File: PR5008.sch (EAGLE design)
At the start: 48 parts

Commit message: beginnings of changes
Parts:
- removed C17: 470pf, resistor:C-USC0805
- removed JP1: (no value), SparkFun-Connectors:M05LOCK
- added C21: 470pF, resistor:C-USC0603
- added JP2: (no value), SparkFun-Connectors:M03LOCK
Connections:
- net GND: now also C21.1, JP2.2; no longer C17.2, JP1.4
- net N$12: now also JP2.1; no longer JP1.3
- net N$22: no longer JP1.1
- net N$29: no longer JP1.2
- net N$34: now also C21.2; no longer C17.1
- net VCC: now also JP2.3; no longer JP1.5
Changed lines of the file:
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@@
 <part name="C16" library="resistor" deviceset="C-US" device="C0603" value="2.2uF"/>
 <part name="GND16" library="SparkFun-Aesthetics" deviceset="GND" device=""/>
-<part name="C17" library="resistor" deviceset="C-US" device="C0805" value="470pf"/>
 <part name="R13" library="resistor" deviceset="R-US_" device="R0603" value="0Ohm"/>
 <part name="GND17" library="SparkFun-Aesthetics" deviceset="GND" device=""/>
@@
 <part name="U$4" library="PR_Libraries" deviceset="SI4831_FM_IC" device=""/>
 <part name="GND18" library="SparkFun-Aesthetics" deviceset="GND" device=""/>
-<part name="JP1" library="SparkFun-Connectors" deviceset="M05" device="LOCK"/>
 <part name="GND19" library="SparkFun-Aesthetics" deviceset="GND" device=""/>
 <part name="P+7" library="supply1" deviceset="VCC" device=""/>
+<part name="JP2" library="SparkFun-Connectors" deviceset="M03" device="LOCK"/>
+<part name="C21" library="resistor" deviceset="C-US" device="C0603" value="470pF"/>
 </parts>
 <sheets>
@@
 </instance>
 <instance part="GND8" gate="1" x="-5.08" y="33.274"/>
-<instance part="GND9" gate="1" x="10.16" y="53.086"/>
+<instance part="GND9" gate="1" x="12.7" y="50.8"/>
 <instance part="L2" gate="G$1" x="84.582" y="76.2" smashed="yes" rot="R270">
 <attribute name="NAME" x="84.582" y="77.978" size="1.778" layer="95" rot="R180"/>
@@
 <instance part="C16" gate="G$1" x="59.436" y="97.536" rot="R90"/>
 <instance part="GND16" gate="1" x="161.798" y="43.18"/>
-<instance part="C17" gate="G$1" x="72.136" y="27.686" smashed="yes">
-<attribute name="NAME" x="65.024" y="28.067" size="1.778" layer="95"/>
-<attribute name="VALUE" x="64.516" y="23.749" size="1.778" layer="96"/>
-</instance>
 <instance part="R13" gate="G$1" x="79.502" y="25.4" smashed="yes" rot="R90">
 <attribute name="NAME" x="85.3694" y="29.464" size="1.778" layer="95" rot="R180"/>
@@
 <instance part="U$4" gate="G$1" x="33.02" y="86.36"/>
 <instance part="GND18" gate="1" x="142.494" y="51.308"/>
-<instance part="JP1" gate="G$1" x="-7.62" y="124.46" rot="R270"/>
-<instance part="GND19" gate="1" x="-5.08" y="110.49"/>
-<instance part="P+7" gate="VCC" x="5.08" y="119.38"/>
+<instance part="GND19" gate="1" x="-43.18" y="93.98"/>
+<instance part="P+7" gate="VCC" x="-35.56" y="101.6"/>
+<instance part="JP2" gate="G$1" x="-43.18" y="106.68" rot="R270"/>
+<instance part="C21" gate="G$1" x="72.136" y="25.146" smashed="yes" rot="R180">
+<attribute name="NAME" x="77.216" y="23.241" size="1.778" layer="95" rot="R180"/>
+<attribute name="VALUE" x="72.136" y="24.765" size="1.778" layer="96" rot="R180"/>
+</instance>
 </instances>
 <busses>
@@
 <pinref part="GND9" gate="1" pin="GND"/>
 <wire x1="12.7" y1="60.96" x2="10.16" y2="60.96" width="0.1524" layer="91"/>
-<wire x1="10.16" y1="60.96" x2="10.16" y2="55.626" width="0.1524" layer="91"/>
+<wire x1="10.16" y1="60.96" x2="12.7" y2="53.34" width="0.1524" layer="91"/>
 <pinref part="U$4" gate="G$1" pin="RFGND"/>
 <pinref part="U$4" gate="G$1" pin="AMI"/>
@@
 </segment>
 <segment>
-<pinref part="C17" gate="G$1" pin="2"/>
 <wire x1="79.502" y1="20.32" x2="75.946" y2="20.32" width="0.1524" layer="91"/>
 <wire x1="75.946" y1="20.32" x2="72.136" y2="20.32" width="0.1524" layer="91"/>
@@
 <junction x="75.946" y="20.32"/>
 <pinref part="R13" gate="G$1" pin="1"/>
+<pinref part="C21" gate="G$1" pin="1"/>
 </segment>
 <segment>
@@
 </segment>
 <segment>
-<pinref part="JP1" gate="G$1" pin="4"/>
-<wire x1="-5.08" y1="116.84" x2="-5.08" y2="113.03" width="0.1524" layer="91"/>
+<wire x1="-43.18" y1="99.06" x2="-43.18" y2="96.52" width="0.1524" layer="91"/>
 <pinref part="GND19" gate="1" pin="GND"/>
+<pinref part="JP2" gate="G$1" pin="2"/>
+<junction x="-43.18" y="99.06"/>
 </segment>
 </net>
@@
 </segment>
 <segment>
-<pinref part="JP1" gate="G$1" pin="5"/>
 <pinref part="P+7" gate="VCC" pin="VCC"/>
-<wire x1="-2.54" y1="116.84" x2="5.08" y2="116.84" width="0.1524" layer="91"/>
+<wire x1="-40.64" y1="99.06" x2="-35.56" y2="99.06" width="0.1524" layer="91"/>
+<pinref part="JP2" gate="G$1" pin="3"/>
+<junction x="-40.64" y="99.06"/>
 </segment>
 </net>
@@
 <pinref part="TUNE" gate="TUNE" pin="2"/>
 <wire x1="-22.86" y1="85.09" x2="-25.4" y2="85.09" width="0.1524" layer="91"/>
-<wire x1="-25.4" y1="85.09" x2="-25.4" y2="66.04" width="0.1524" layer="91"/>
+<wire x1="-25.4" y1="85.09" x2="-25.4" y2="83.82" width="0.1524" layer="91"/>
 <pinref part="U$4" gate="G$1" pin="TUNE2"/>
 <junction x="12.7" y="78.74"/>
-<wire x1="-7.62" y1="93.98" x2="-22.86" y2="93.98" width="0.1524" layer="91"/>
-<wire x1="-22.86" y1="93.98" x2="-22.86" y2="85.09" width="0.1524" layer="91"/>
-<pinref part="JP1" gate="G$1" pin="3"/>
-<wire x1="-7.62" y1="93.98" x2="-7.62" y2="116.84" width="0.1524" layer="91"/>
+<pinref part="JP2" gate="G$1" pin="1"/>
+<wire x1="-25.4" y1="83.82" x2="-25.4" y2="66.04" width="0.1524" layer="91"/>
+<wire x1="-45.72" y1="99.06" x2="-45.72" y2="83.82" width="0.1524" layer="91"/>
+<wire x1="-45.72" y1="83.82" x2="-25.4" y2="83.82" width="0.1524" layer="91"/>
 </segment>
 </net>
@@
 <pinref part="R10" gate="G$1" pin="2"/>
 <wire x1="-15.24" y1="69.596" x2="-15.24" y2="68.58" width="0.1524" layer="91"/>
-<wire x1="-41.91" y1="116.84" x2="-41.91" y2="74.93" width="0.1524" layer="91"/>
-<wire x1="-41.91" y1="74.93" x2="-15.24" y2="74.93" width="0.1524" layer="91"/>
-<wire x1="-15.24" y1="74.93" x2="-15.24" y2="68.58" width="0.1524" layer="91"/>
-<pinref part="JP1" gate="G$1" pin="2"/>
-<wire x1="-10.16" y1="116.84" x2="-41.91" y2="116.84" width="0.1524" layer="91"/>
 </segment>
 </net>
@@
 <pinref part="U$4" gate="G$1" pin="TUNE1"/>
 <junction x="12.7" y="81.28"/>
-<pinref part="JP1" gate="G$1" pin="1"/>
-<wire x1="-12.7" y1="116.84" x2="-12.7" y2="91.44" width="0.1524" layer="91"/>
-<wire x1="-12.7" y1="91.44" x2="-15.24" y2="91.44" width="0.1524" layer="91"/>
 <wire x1="-15.24" y1="91.44" x2="-15.24" y2="88.9" width="0.1524" layer="91"/>
 </segment>
@@
 <segment>
 <pinref part="R13" gate="G$1" pin="2"/>
-<pinref part="C17" gate="G$1" pin="1"/>
 <wire x1="79.502" y1="30.48" x2="75.692" y2="30.48" width="0.1524" layer="91"/>
 <wire x1="75.692" y1="30.48" x2="72.136" y2="30.48" width="0.1524" layer="91"/>
@@
 <junction x="75.692" y="30.48"/>
 <pinref part="LID" gate="P" pin="P"/>
-</segment>
-</net>
+<pinref part="C21" gate="G$1" pin="2"/>
+</segment>
+</net>

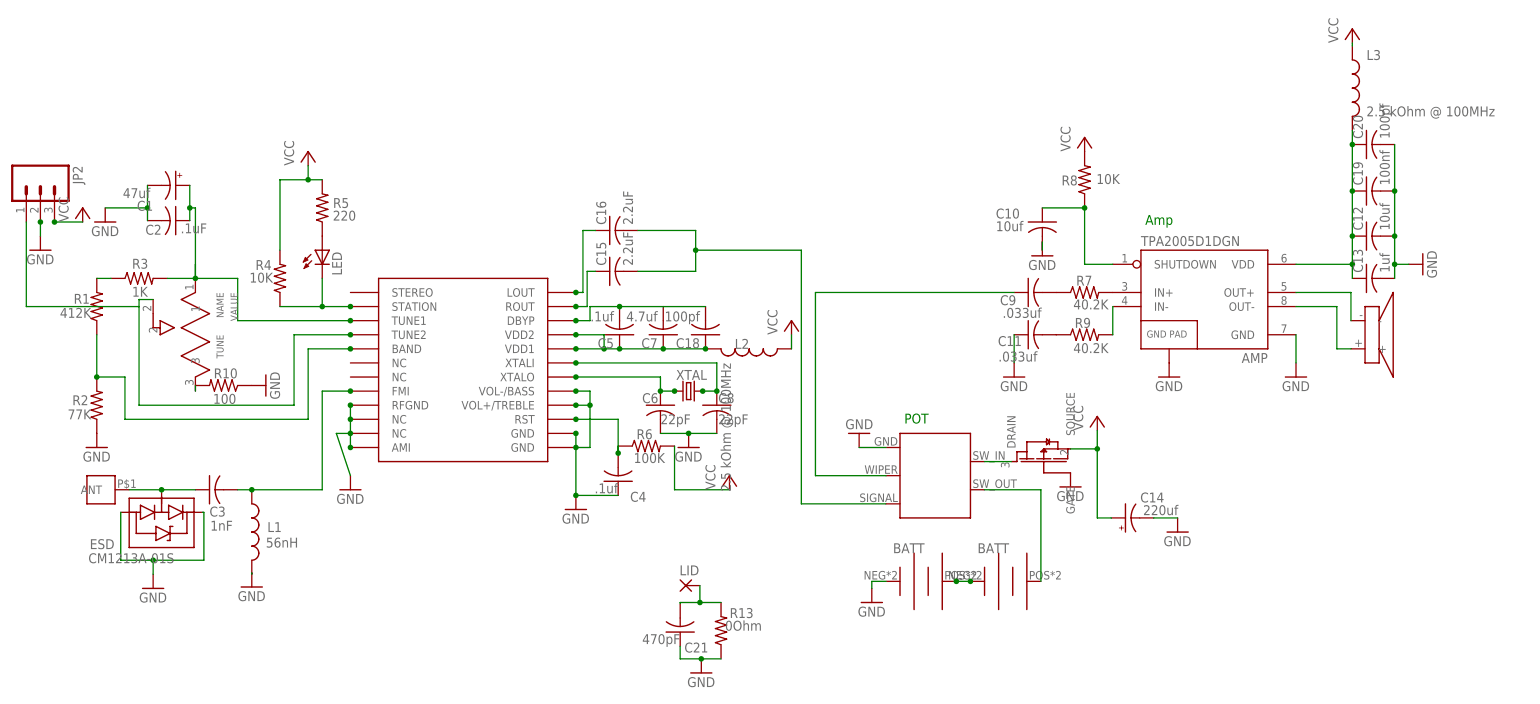
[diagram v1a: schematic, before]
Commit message: sch update + reset pin screwup
major update to the sch - cleaned it up significantly
also fixed screwup at the reset pin, which was a bug in pr5007
some small brd changes too, mostly around the trimpot
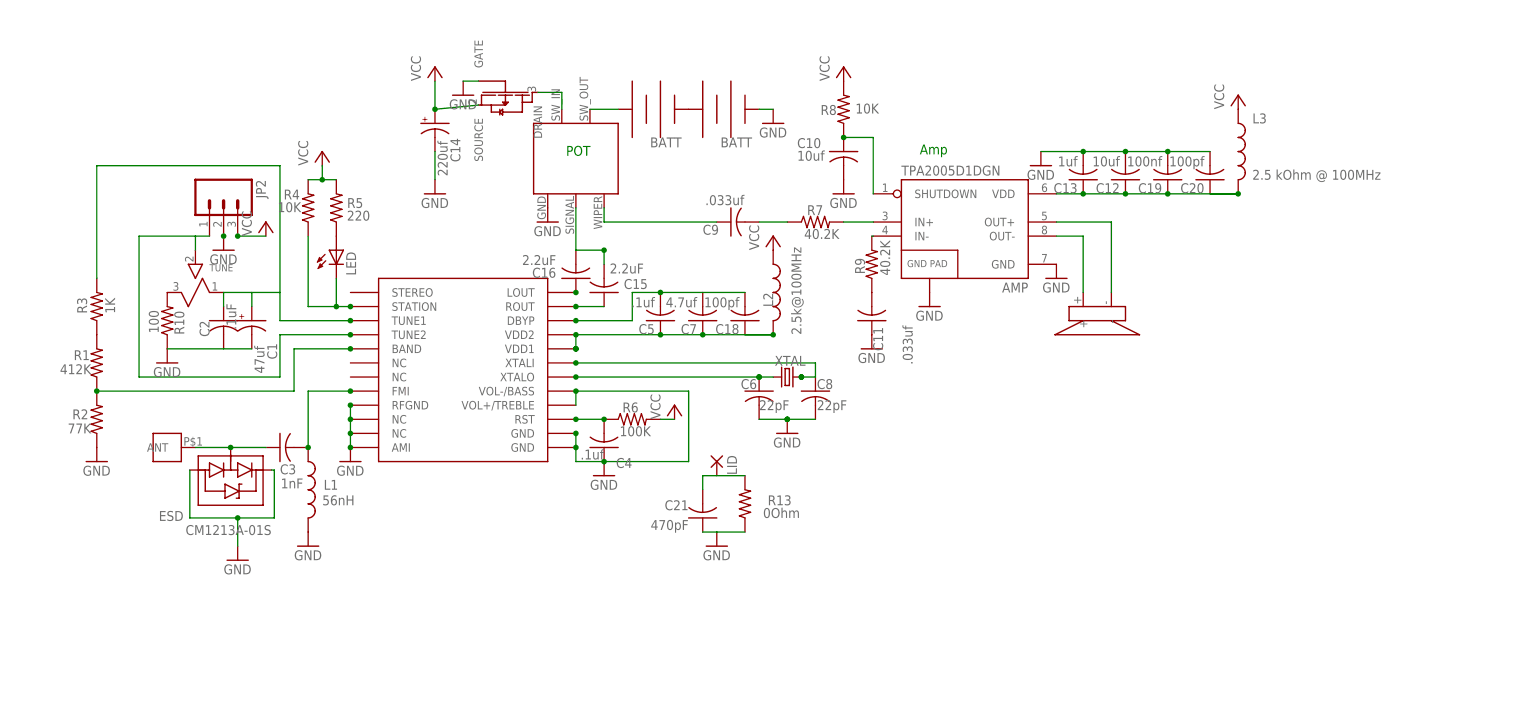
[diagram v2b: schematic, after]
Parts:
- L2: value 2.5 kOhm @ 100MHz -> 2.5k@100MHz
- TUNE: value TUNE -> 10k
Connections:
- new net N$35: R3.2
- net N$22: no longer R3.2
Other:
- moved on the sheet: AMP, C1, C10, C11, C12, C13, C14, C15, C16, C18, C19, C2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

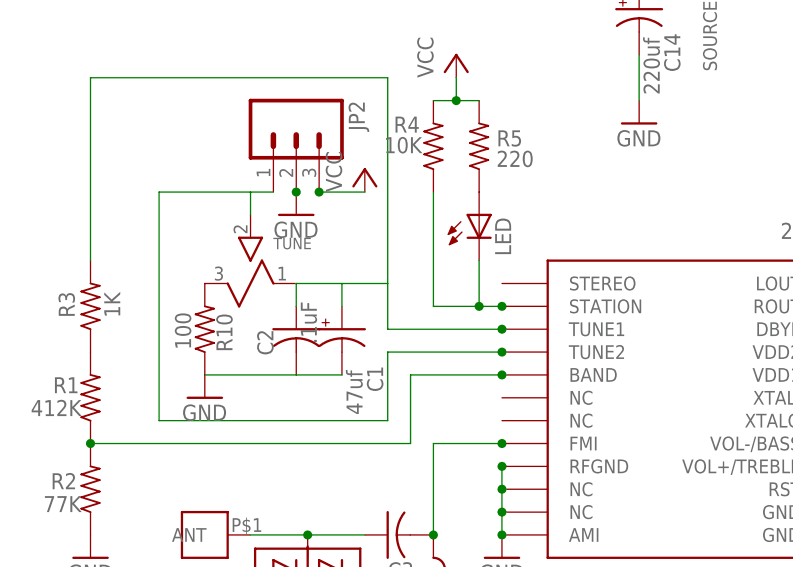
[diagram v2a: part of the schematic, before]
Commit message: Updates and Fixes
Small changes, clearing Osh Park design rules
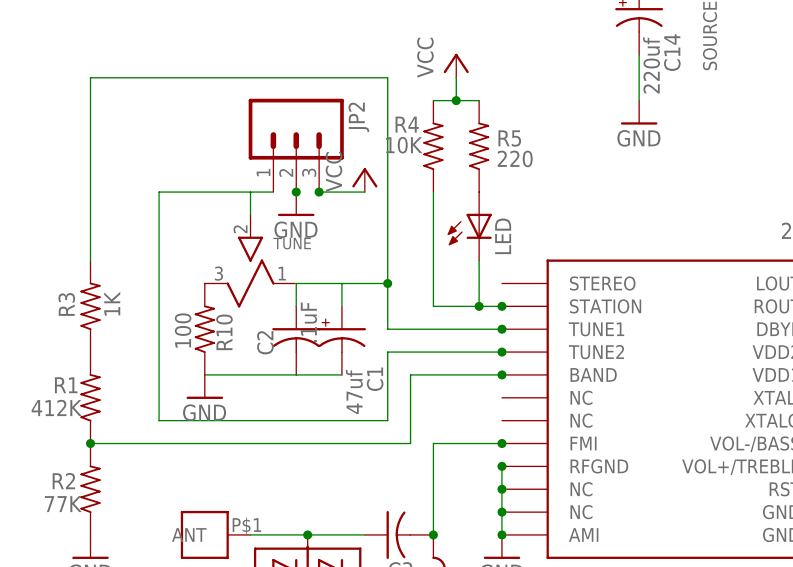
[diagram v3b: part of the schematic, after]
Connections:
- removed net N$35: R3.2
- net N$22: now also R3.2
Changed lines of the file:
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@@
 <?xml version="1.0" encoding="utf-8"?>
 <!DOCTYPE eagle SYSTEM "eagle.dtd">
-<eagle version="6.6.0">
+<eagle version="6.4">
 <drawing>
 <settings>
@@
 <pinref part="C2" gate="G$1" pin="1"/>
 <wire x1="-10.16" y1="83.82" x2="-10.16" y2="86.36" width="0.1524" layer="91"/>
+<pinref part="R3" gate="G$1" pin="2"/>
+<wire x1="-33.02" y1="88.9" x2="-33.02" y2="109.22" width="0.1524" layer="91"/>
+<wire x1="-33.02" y1="109.22" x2="0" y2="109.22" width="0.1524" layer="91"/>
+<wire x1="0" y1="109.22" x2="0" y2="86.36" width="0.1524" layer="91"/>
+<junction x="0" y="86.36"/>
 </segment>
 </net>
@@
 </segment>
 </net>
-<net name="N$35" class="0">
-<segment>
-<pinref part="R3" gate="G$1" pin="2"/>
-<wire x1="-33.02" y1="88.9" x2="-33.02" y2="109.22" width="0.1524" layer="91"/>
-<wire x1="-33.02" y1="109.22" x2="0" y2="109.22" width="0.1524" layer="91"/>
-<wire x1="0" y1="109.22" x2="0" y2="86.36" width="0.1524" layer="91"/>
-</segment>
-</net>
